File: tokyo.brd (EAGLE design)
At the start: 115 x 34 mm, 50 parts, among them J1 254-2X5F, J2 254-2X5M, P1 9774050151, P2 9774050151, P3 9774050151, P4 9774050151, Q1 STD6N95K5, T1 750313823, U1 UCC28710, X1 508-1X3B

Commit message: Changed R3 to 330 (LD1 was too dim). Corrected BOM (LD1 should be a green LED).
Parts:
- R3: value 1k -> 330
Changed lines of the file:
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@@
 <?xml version="1.0" encoding="utf-8"?>
 <!DOCTYPE eagle SYSTEM "eagle.dtd">
-<eagle version="7.2.0">
+<eagle version="7.3.0">
 <drawing>
 <settings>
@@
 <attribute name="NAME" x="83.815" y="26.3156" size="1.016" layer="26" ratio="10" rot="SMR90"/>
 </element>
-<element name="R3" library="resistors" package="0603" value="1k" x="85.74" y="6.63" smashed="yes" rot="MR180">
+<element name="R3" library="resistors" package="0603" value="330" x="85.74" y="6.63" smashed="yes" rot="MR180">
 <attribute name="NAME" x="87.0754" y="7.724" size="1.016" layer="26" ratio="10" rot="SMR0"/>
 </element>

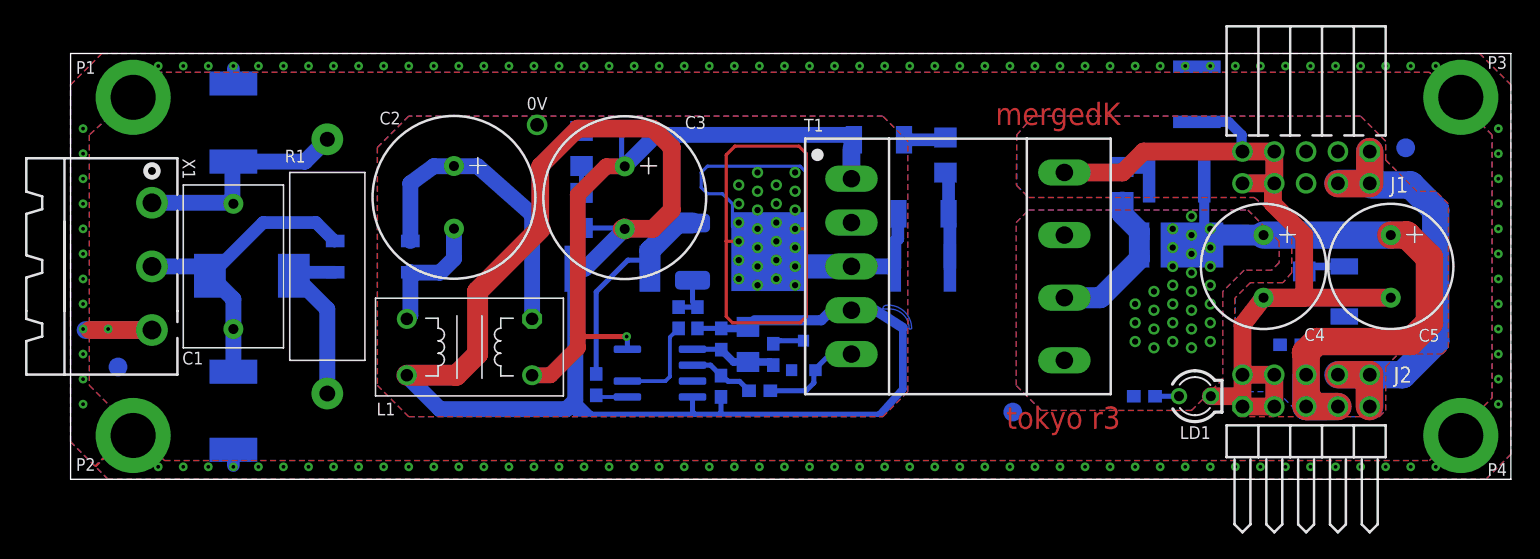
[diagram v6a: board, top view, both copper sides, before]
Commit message: Incorporated changes required for EMC tests: replaced transzorb with varistor, changed position of line choke.
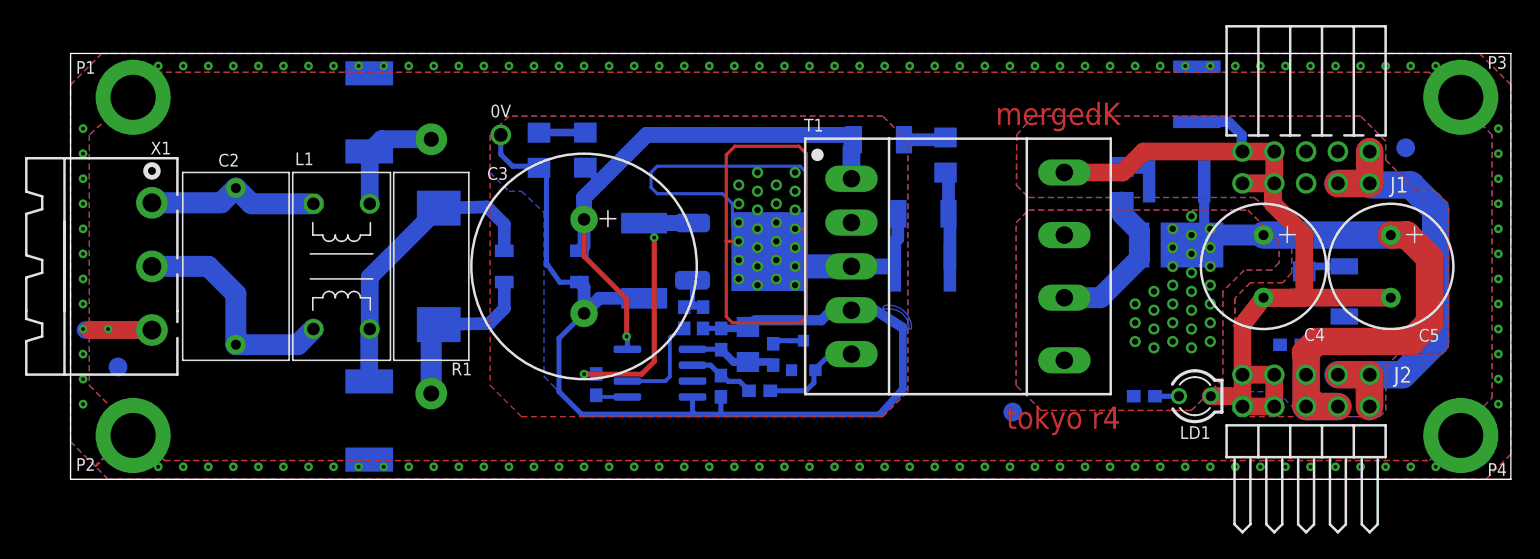
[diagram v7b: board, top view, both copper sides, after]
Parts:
- removed C1: 220n/275Vac, capacitors:14X8
- removed D7: SMCJ400CA, supressors:DO-214AB
- added R15: CU4032K275G2, supressors:4032
- C2: value 22u/400V -> 330n/275Vac; device capacitors:D13 -> capacitors:15X8.5
- C3: value 22u/400V -> 33u/400V; device capacitors:D13 -> capacitors:D18
- moved C2 18.3 mm to (13.2, 17.0), turned to 270 degrees
- moved D6 13.5 mm to (37.6, 17.0)
- moved L1 12.1 mm to (21.6, 17.0), turned to 90 degrees
- moved C13 10.9 mm to (23.9, 29.3)
- moved C12 10.9 mm to (23.9, 4.70)
- moved R1 8.30 mm to (28.8, 17.0)
- moved C3 6.38 mm to (41.0, 17.0)
- moved R13 5.88 mm to (37.4, 26.3)
- moved 0V 3.01 mm to (34.4, 27.5)
- moved R11 2.62 mm to (45.8, 17.5), turned to 90 degrees
- moved R10 0.45 mm to (49.0, 12.9)
- moved R9 0.45 mm to (50.5, 12.9)
- moved R14 0.33 mm to (41.1, 26.3), turned to 90 degrees
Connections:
- removed net N$20: C2.2, D6.2, L1.4
- removed net N$21: C2.1, D6.1, L1.1
- new net N$19: C2.1, L1.1, X1.1
- new net N$22: C2.2, L1.4, X1.2
- net 0V: now also D6.2; no longer L1.3
- net N$1: now also L1.2; no longer C1.1, X1.1
- net N$2: now also L1.3, R15.2; no longer C1.2, D7.P$1, X1.2
- net N$4: now also R15.1; no longer D7.P$2
- net N$9: now also D6.1; no longer L1.2
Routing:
- net 0V: track 136.4 -> 85.5 mm
- net N$21: track 24.6 -> 0.00 mm
- net N$22: track 0.00 -> 18.4 mm
- net N$19: track 0.00 -> 13.9 mm
- net N$20: track 10.2 -> 0.00 mm
- net N$9: track 55.5 -> 46.5 mm
- net N$1: track 18.1 -> 9.55 mm
- net N$11: track 88.0 -> 96.0 mm
- net N$12: track 18.3 -> 22.1 mm, vias 0 -> 2
- net EARTH: track 14.7 -> 12.2 mm
- net N$2: track 25.7 -> 24.1 mm
- net N$7: track 2.14 -> 3.71 mm
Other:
- board text added: "tokyo r4"
- board text removed: "tokyo r3"

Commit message: Changed R15 to 10 k due to bright LED usage. Renumbered all components.
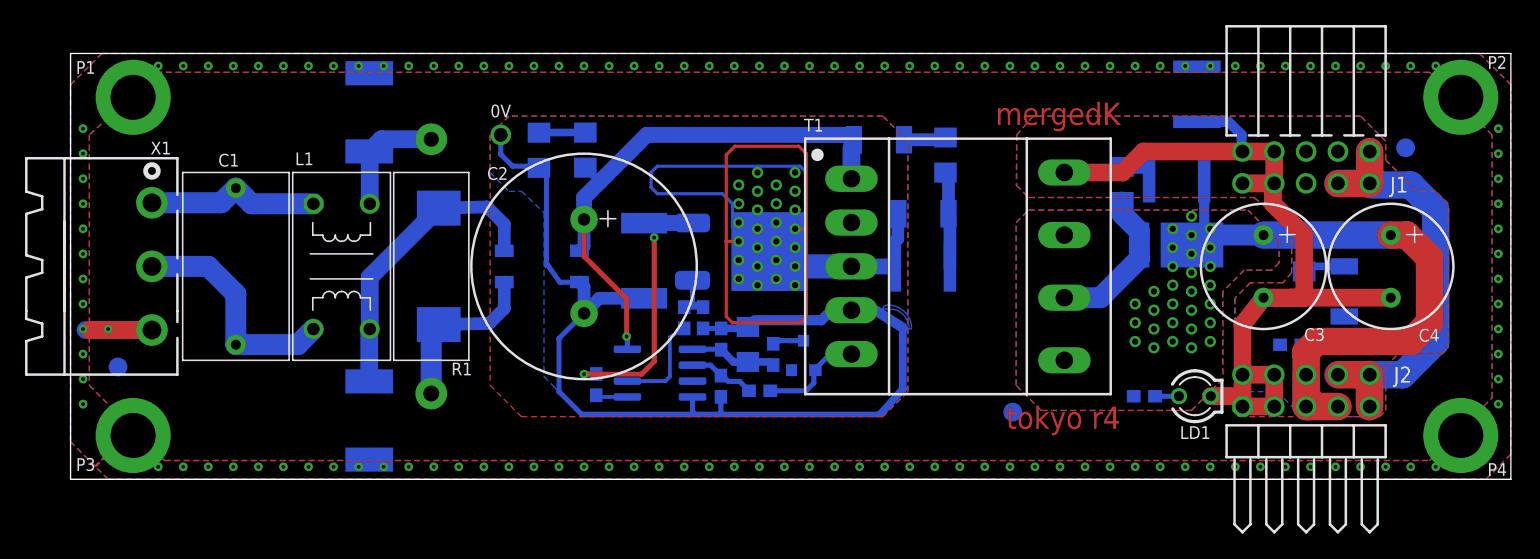
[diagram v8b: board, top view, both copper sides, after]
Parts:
- removed C13: 2200p/250Vac, capacitors:2211
- added C1: 330n/275Vac, capacitors:15X8.5
- C2: value 330n/275Vac -> 33u/400V; device capacitors:15X8.5 -> capacitors:D18
- C3: value 33u/400V -> 1500u; device capacitors:D18 -> capacitors:D10
- C5: value 1500u -> 1000p/250Vac; device capacitors:D10 -> capacitors:1812
- C6: value 100n -> 2200p/250Vac; device capacitors:0603 -> capacitors:2211
- C9: value 1000p/250Vac -> 100n; device capacitors:1812 -> capacitors:0603
- D1: value 1SMB5919BT3G -> MURS360S
- D2: value PDS1040L -> SMBJ85A; device diodes:POWERDI5 -> supressors:DO-214AA
- D3: value SMBJ85A -> PDS1040L; device supressors:DO-214AA -> diodes:POWERDI5
- D4: value MURS360S -> HD06; device diodes:DO-214AA -> diodes:MINIDIP
- D5: value BAS21 -> 1SMB5919BT3G; device diodes:SOT23 -> diodes:DO-214AA
- D6: value HD06 -> BAS21; device diodes:MINIDIP -> diodes:SOT23
- R11: value 0.5/0.8W -> 39; device resistors:2512 -> resistors:0603
- R13: value 332k -> 24k9; device resistors:1206 -> resistors:0603
- R14: value 332k -> 121k; device resistors:1206 -> resistors:0603
- R15: value CU4032K275G2 -> 10k; device supressors:4032 -> resistors:0603
- R2: value 1 -> 332k
- R3: value 330 -> 332k; device resistors:0603 -> resistors:1206
- R4: value 39 -> 130
- R5: value 130 -> 39
- R6: value 39 -> 1; device resistors:0603 -> resistors:1206
- R7: value 121k -> 0.5/0.8W; device resistors:0603 -> resistors:2512
- R8: value 24k9 -> CU4032K275G2; device resistors:0603 -> supressors:4032
- moved P2 109.4 mm to (111.0, 30.5)
- moved P3 109.4 mm to (5.00, 3.50)
- moved C6 75.9 mm to (23.9, 29.3), turned to 270 degrees
- moved FIDUCIAL2 71.5 mm to (3.79, 8.97)
- moved FIDUCIAL3 71.5 mm to (75.2, 5.37)
- moved R2 58.0 mm to (41.1, 26.3), turned to 90 degrees
- moved R15 57.3 mm to (85.7, 6.63), turned to 180 degrees
- moved C3 54.2 mm to (95.2, 17.0)
- moved R3 52.2 mm to (37.4, 26.3), turned to 270 degrees
- moved C11 45.5 mm to (97.4, 10.7), turned to 0 degrees
- moved D5 43.5 mm to (101.7, 15.0), turned to 270 degrees
- moved R6 43.1 mm to (98.5, 18.0), turned to 270 degrees
- moved D1 39.1 mm to (64.5, 27.1), turned to 180 degrees
- moved D4 28.8 mm to (37.6, 17.0), turned to 90 degrees
- moved C2 27.8 mm to (41.0, 17.0), turned to 0 degrees
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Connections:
- net +5V/1: now also C11.1, C3.1, C7.2, D3.3, R15.1, R6.1; no longer C5.1, C6.1, C8.2, D2.3, R2.1, R3.1
- net 0V: now also C2.2, C9.2, D4.2, R3.2, R7.1; no longer C11.2, C3.2, D6.2, R11.1, R8.2
- net 0V/1: now also C11.2, C3.2, C5.1, D5.2; no longer C5.2, C6.2, C7.1, D1.2
- net EARTH: now also C5.2, C6.1; no longer C13.1, C7.2
- net N$1: now also C6.2; no longer C13.2
- net N$10: now also D1.2, R4.1; no longer D4.2, R5.1
- net N$11: now also C8.2, D2.1; no longer C9.2, D3.1
- net N$12: now also R7.2; no longer R11.2
- net N$15: now also C9.1, R11.1; no longer C11.1, R6.1
- net N$16: now also D5.1, R6.2; no longer D1.1, R2.2
- net N$17: now also C8.1, D2.2, R4.2; no longer C9.1, D3.2, R5.2
- net N$18: now also R13.1, R14.2; no longer R7.2, R8.1
- net N$19: now also C1.1; no longer C2.1
- net N$2: now also D4.4, R8.2; no longer D6.4, R15.2
- net N$22: now also C1.2; no longer C2.2
- net N$26: now also D6.3, R11.2; no longer D5.3, R6.2
- net N$3: now also D6.1, R14.1; no longer D5.1, R7.1
- net N$4: now also D4.3, R8.1; no longer D6.3, R15.1
- net N$5: now also R15.2; no longer R3.2
- net N$6: now also C7.1, R5.2; no longer C8.1, R4.2
- net N$7: now also R2.2, R3.1; no longer R13.1, R14.2
- net N$8: now also D3.1, D3.2, R5.1; no longer D2.1, D2.2, R4.1
- net N$9: now also C2.1, D1.1, R2.1; no longer C3.1, D6.1, R14.1
